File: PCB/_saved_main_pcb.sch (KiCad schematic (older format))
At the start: 17 parts, among them P1 SEN, P2 SRV, P3 PWR, P4 LED, P5 M1, P6 M2, P7 CONN_02X03, P8 CONN_02X03, Q1 5LN01SP, U1 Teensy_3.1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

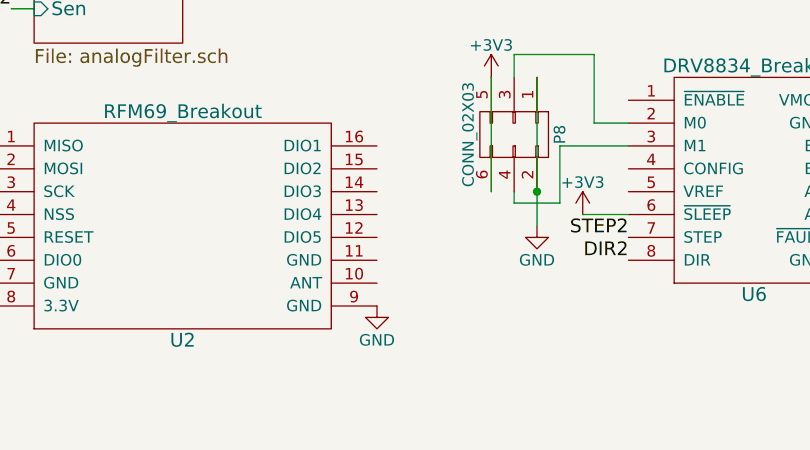
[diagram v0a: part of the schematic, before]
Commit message: Pulled in RFM69 library, modified to support teensy
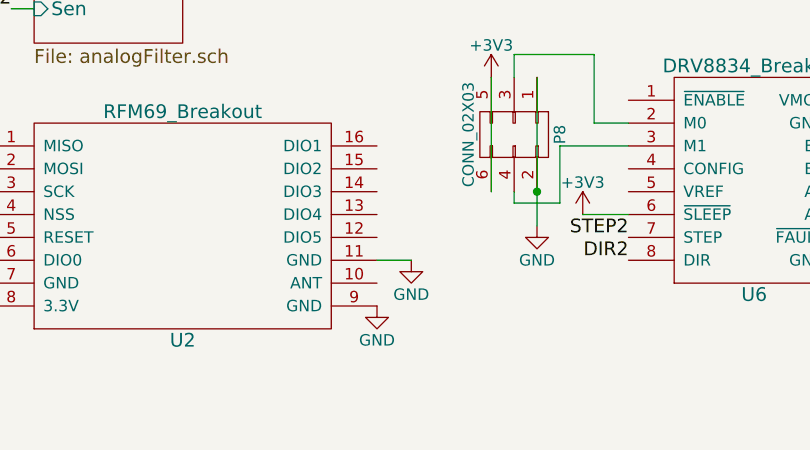
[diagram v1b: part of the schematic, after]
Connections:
- net GND: now also U2.11 (GND)
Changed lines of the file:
@@
 Wire Wire Line
 	2850 6100 2850 5650
+$Comp
+L GND #PWR?
+U 1 1 594A8840
+P 7550 5350
+F 0 "#PWR?" H 7550 5100 50  0001 C CNN
+F 1 "GND" H 7550 5200 50  0000 C CNN
+F 2 "" H 7550 5350 50  0000 C CNN
+F 3 "" H 7550 5350 50  0000 C CNN
+	1    7550 5350
+	1    0    0    -1
+$EndComp
+Wire Wire Line
+	7400 5350 7550 5350
 $EndSCHEMATC
